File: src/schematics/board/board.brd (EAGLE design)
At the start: 50.8 x 35.6 mm, 23 parts, among them P1 PN61729-S, Q1 12MHz, U1 MCP17003302E/TO, U2 PIC18LF14K50-E-P

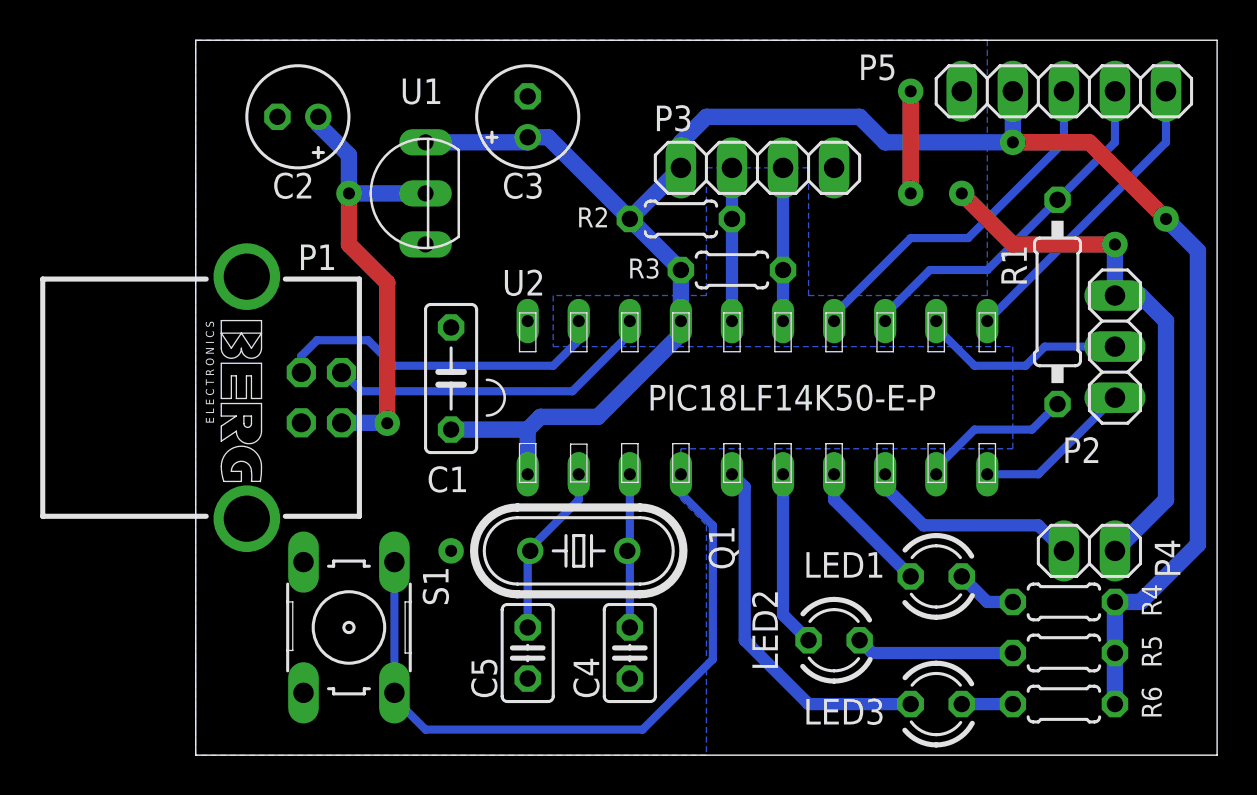
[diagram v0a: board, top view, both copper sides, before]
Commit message: Added UART pull-ups
Added pull-ups to the UART port, so that there are never mistaken signals.
They are not critical, but may help in keeping consistent values,
especially for the receiver.

Andrea Zoppi
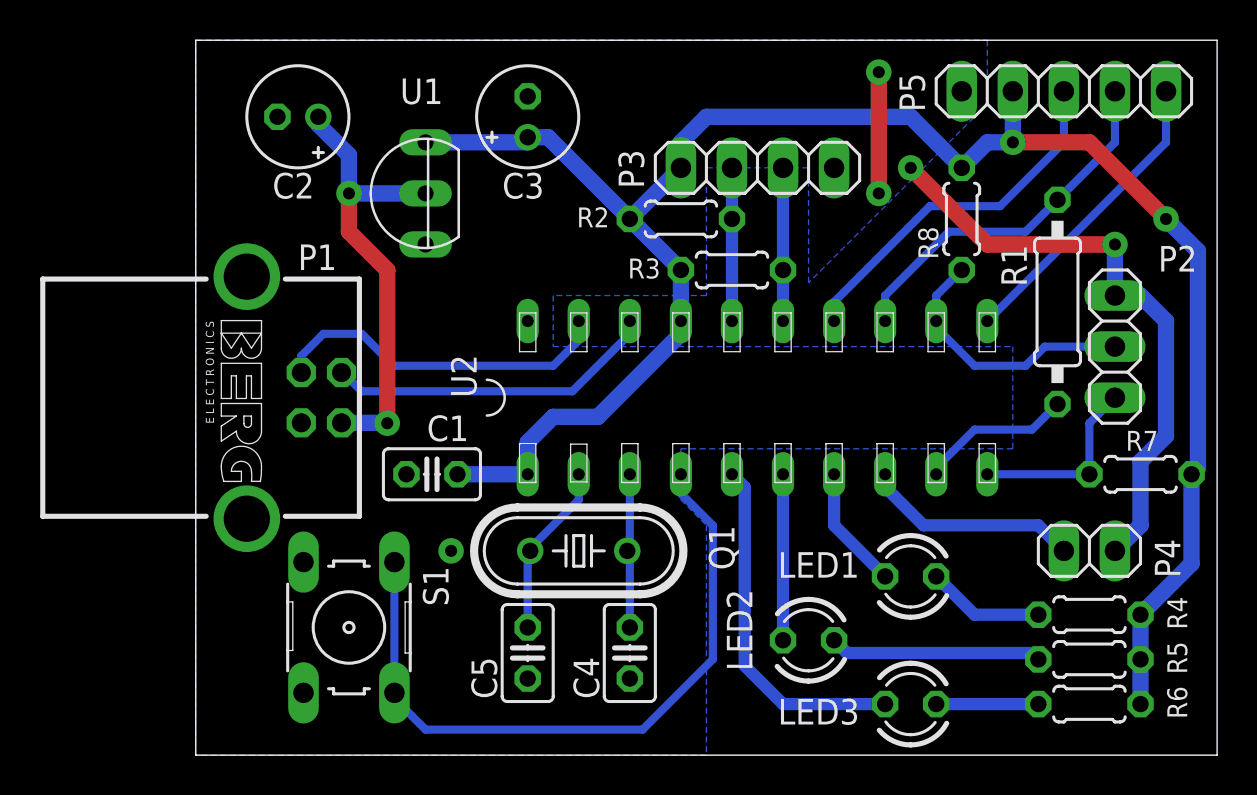
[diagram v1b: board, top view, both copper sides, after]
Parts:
- added R7, R8: 100k, rcl:0204/5
- C1: device rcl:C050-025X075 -> rcl:C025-025X050
- moved C1 4.86 mm to (11.7, 14.0), turned to 180 degrees
- moved R4 1.42 mm to (44.5, 6.99)
- moved R5 1.31 mm to (44.5, 4.76)
- moved R6 1.27 mm to (44.5, 2.54)
- moved LED2 1.27 mm to (30.5, 5.71)
- moved LED1 1.27 mm to (35.6, 8.89)
- moved LED3 1.27 mm to (35.6, 2.54)
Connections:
- net +3V3: now also R7.2, R8.2
- net RX: now also R8.1
- net TX: now also R7.1
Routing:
- net GND: track 31.8 -> 35.9 mm
- net RX: track 10.4 -> 13.5 mm
- net N$5: track 3.07 -> 5.87 mm
- net N$4: track 7.88 -> 10.6 mm
- net N$1: track 2.54 -> 5.08 mm
- net TX: track 7.93 -> 9.42 mm
- net +3V3: track 95.9 -> 95.0 mm
- net SDIO: track 17.8 -> 18.4 mm
- net RED: track 18.1 -> 17.6 mm
- net GREEN: track 6.66 -> 6.13 mm
- net YELLOW: track 8.78 -> 8.26 mm
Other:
- board text added: "1"
- board text added: "3V3"
- board text added: "5"
- board text added: "GND"
- board text added: "IN"
- board text added: "QA"
- board text added: "QB"
- board text added: "RX"
- board text added: "TX"

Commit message: Added user button pull-up
A pull-up resistor was added to the user button, because the built-in weak
pull-up of the MCU does not work properly at power-up.

Andrea Zoppi
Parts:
- added R9: 47k, rcl:0204/5
- R7, R8: value 100k -> 47k
- moved S1 1.80 mm to (6.35, 5.08)
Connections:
- net +3V3: now also R9.2
- net RST: now also R9.1
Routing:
- net +3V3: track 95.0 -> 102.7 mm
- net RST: track 34.6 -> 35.3 mm
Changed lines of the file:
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@@
 <layer number="27" name="tValues" color="7" fill="1" visible="yes" active="yes"/>
 <layer number="28" name="bValues" color="7" fill="1" visible="yes" active="yes"/>
-<layer number="29" name="tStop" color="7" fill="3" visible="yes" active="yes"/>
-<layer number="30" name="bStop" color="7" fill="6" visible="yes" active="yes"/>
-<layer number="31" name="tCream" color="7" fill="4" visible="yes" active="yes"/>
+<layer number="29" name="tStop" color="7" fill="3" visible="no" active="yes"/>
+<layer number="30" name="bStop" color="7" fill="6" visible="no" active="yes"/>
+<layer number="31" name="tCream" color="7" fill="4" visible="no" active="yes"/>
 <layer number="32" name="bCream" color="7" fill="5" visible="no" active="yes"/>
 <layer number="33" name="tFinish" color="6" fill="3" visible="no" active="yes"/>
@@
 <attribute name="NAME" x="25.527" y="11.43" size="1.27" layer="25" ratio="10" rot="R270"/>
 </element>
-<element name="S1" library="switch-omron" package="B3F-10XX" value="" x="7.62" y="6.35" rot="R270">
-<attribute name="OC_NEWARK" value="36M3542" x="-25.4" y="-12.7" size="1.778" layer="27" rot="R270" display="off"/>
-<attribute name="MPN" value="B3F-1000" x="-25.4" y="-12.7" size="1.778" layer="27" rot="R270" display="off"/>
-<attribute name="MF" value="" x="-25.4" y="-12.7" size="1.778" layer="27" rot="R270" display="off"/>
-<attribute name="OC_FARNELL" value="176432" x="-25.4" y="-12.7" size="1.778" layer="27" rot="R270" display="off"/>
+<element name="S1" library="switch-omron" package="B3F-10XX" value="" x="6.35" y="5.08" smashed="yes" rot="R270">
+<attribute name="OC_NEWARK" value="36M3542" x="-26.67" y="-13.97" size="1.778" layer="27" rot="R270" display="off"/>
+<attribute name="MPN" value="B3F-1000" x="-26.67" y="-13.97" size="1.778" layer="27" rot="R270" display="off"/>
+<attribute name="MF" value="" x="-26.67" y="-13.97" size="1.778" layer="27" rot="R270" display="off"/>
+<attribute name="OC_FARNELL" value="176432" x="-26.67" y="-13.97" size="1.778" layer="27" rot="R270" display="off"/>
+<attribute name="NAME" x="2.667" y="4.572" size="1.27" layer="25" ratio="10" rot="R90"/>
+<attribute name="VALUE" x="1.27" y="8.128" size="1.27" layer="27" ratio="10" rot="R270"/>
 </element>
 <element name="P2" library="pinhead" package="1X03" value="" x="45.72" y="20.32" smashed="yes" rot="R90">
@@
 </element>
 <element name="C4" library="rcl" package="C025-025X050" value="15p" x="21.59" y="5.08" smashed="yes" rot="R270">
-<attribute name="NAME" x="20.066" y="2.794" size="1.27" layer="25" ratio="10" rot="R90"/>
+<attribute name="NAME" x="20.8915" y="0.889" size="1.27" layer="25" ratio="10"/>
 </element>
 <element name="C5" library="rcl" package="C025-025X050" value="15p" x="16.51" y="5.08" smashed="yes" rot="R270">
-<attribute name="NAME" x="14.986" y="2.794" size="1.27" layer="25" ratio="10" rot="R90"/>
+<attribute name="NAME" x="15.494" y="0.889" size="1.27" layer="25" ratio="10"/>
 </element>
 <element name="R1" library="rcl" package="0207/10" value="100" x="42.8625" y="22.5425" smashed="yes" rot="R90">
@@
 <attribute name="VALUE" x="41.91" y="6.985" size="1.27" layer="27"/>
 </element>
-<element name="R7" library="rcl" package="0204/5" value="100k" x="46.99" y="13.97" smashed="yes">
+<element name="R7" library="rcl" package="0204/5" value="47k" x="46.99" y="13.97" smashed="yes">
 <attribute name="NAME" x="46.2534" y="15.1384" size="0.9906" layer="25" ratio="10"/>
 </element>
-<element name="R8" library="rcl" package="0204/5" value="100k" x="38.1" y="26.67" smashed="yes" rot="R90">
+<element name="R8" library="rcl" package="0204/5" value="47k" x="38.1" y="26.67" smashed="yes" rot="R90">
 <attribute name="NAME" x="36.9316" y="24.6634" size="0.9906" layer="25" ratio="10" rot="R90"/>
+</element>
+<element name="R9" library="rcl" package="0204/5" value="47k" x="12.7" y="3.81" smashed="yes" rot="R90">
+<attribute name="NAME" x="11.5316" y="3.0734" size="0.9906" layer="25" ratio="10" rot="R90"/>
 </element>
 </elements>
@@
 <wire x1="39.37" y1="25.4" x2="35.56" y2="29.21" width="0.8128" layer="1"/>
 <via x="35.56" y="29.21" extent="1-16" drill="0.6" diameter="1.27" shape="octagon"/>
-<via x="12.7" y="10.16" extent="1-16" drill="0.6" diameter="1.27" shape="octagon"/>
+<via x="19.05" y="6.985" extent="1-16" drill="0.6" diameter="1.27" shape="octagon"/>
 <polygon width="0.3048" layer="16">
 <vertex x="25.4" y="0"/>
@@
 <contactref element="R8" pad="2"/>
 <contactref element="R7" pad="2"/>
+<contactref element="R9" pad="2"/>
+<wire x1="13.0175" y1="13.97" x2="13.0175" y2="6.6675" width="0.8128" layer="16"/>
+<wire x1="13.0175" y1="6.6675" x2="12.7" y2="6.35" width="0.8128" layer="16"/>
 </signal>
 <signal name="N$2">
@@
 <wire x1="25.7175" y1="11.43" x2="24.13" y2="13.0175" width="0.4064" layer="16"/>
 <wire x1="24.13" y1="13.0175" x2="24.13" y2="13.97" width="0.4064" layer="16"/>
-<wire x1="9.8806" y1="9.6012" x2="9.8806" y2="3.0988" width="0.4064" layer="16"/>
-<wire x1="9.8806" y1="3.0988" x2="9.8806" y2="2.8194" width="0.6096" layer="16"/>
-<wire x1="9.8806" y1="2.8194" x2="11.43" y2="1.27" width="0.4064" layer="16"/>
-<wire x1="11.43" y1="1.27" x2="22.225" y2="1.27" width="0.4064" layer="16"/>
+<wire x1="8.6106" y1="8.3312" x2="8.6106" y2="1.8288" width="0.4064" layer="16"/>
+<wire x1="8.89" y1="1.27" x2="22.225" y2="1.27" width="0.4064" layer="16"/>
 <wire x1="22.225" y1="1.27" x2="25.7175" y2="4.7625" width="0.4064" layer="16"/>
+<contactref element="R9" pad="1"/>
+<wire x1="8.6106" y1="1.8288" x2="8.6106" y2="1.5494" width="0.4064" layer="16"/>
+<wire x1="8.6106" y1="1.5494" x2="8.89" y2="1.27" width="0.4064" layer="16"/>
+<wire x1="8.89" y1="1.27" x2="12.7" y2="1.27" width="0" layer="19" extent="16-16"/>
 </signal>
 <signal name="TX">

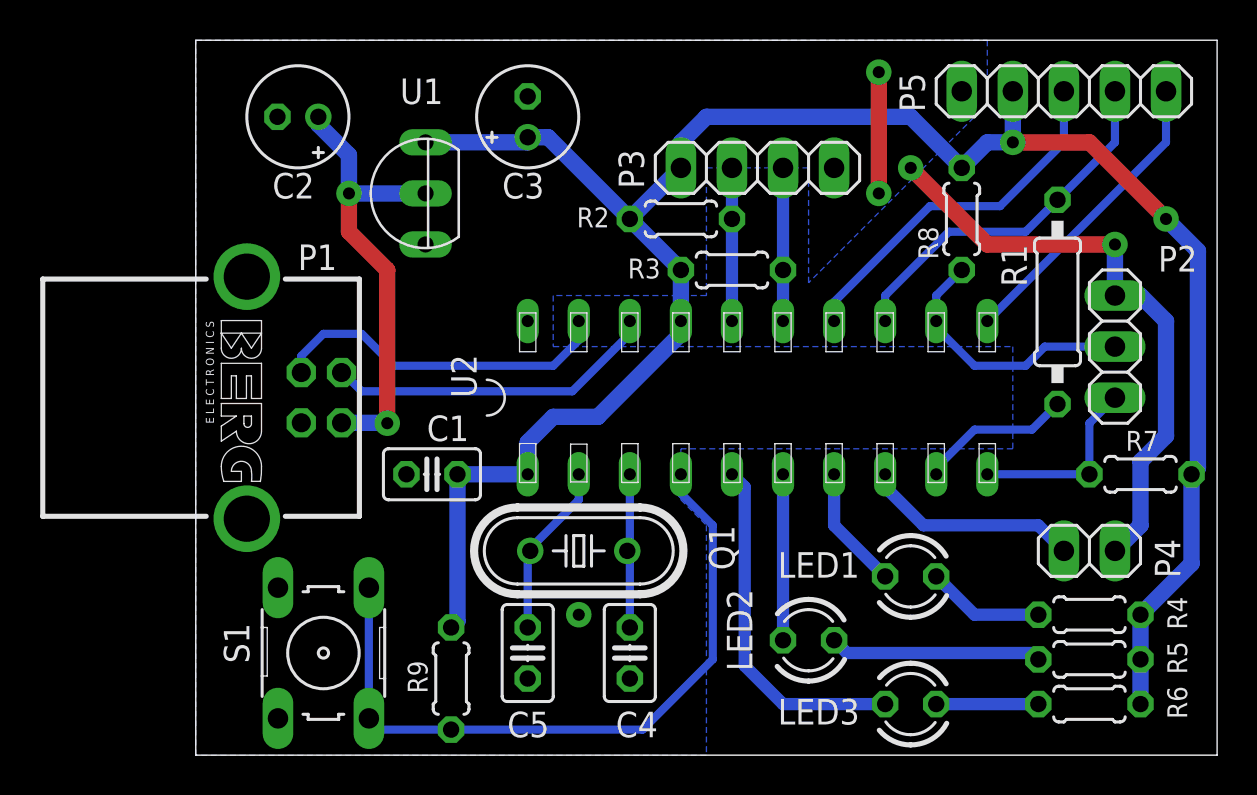
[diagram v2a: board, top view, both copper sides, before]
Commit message: Minor PCB fixes
Changed resistor values so that performance is improved, and the PIC
inputs can read correct pull-up values.

Andrea Zoppi
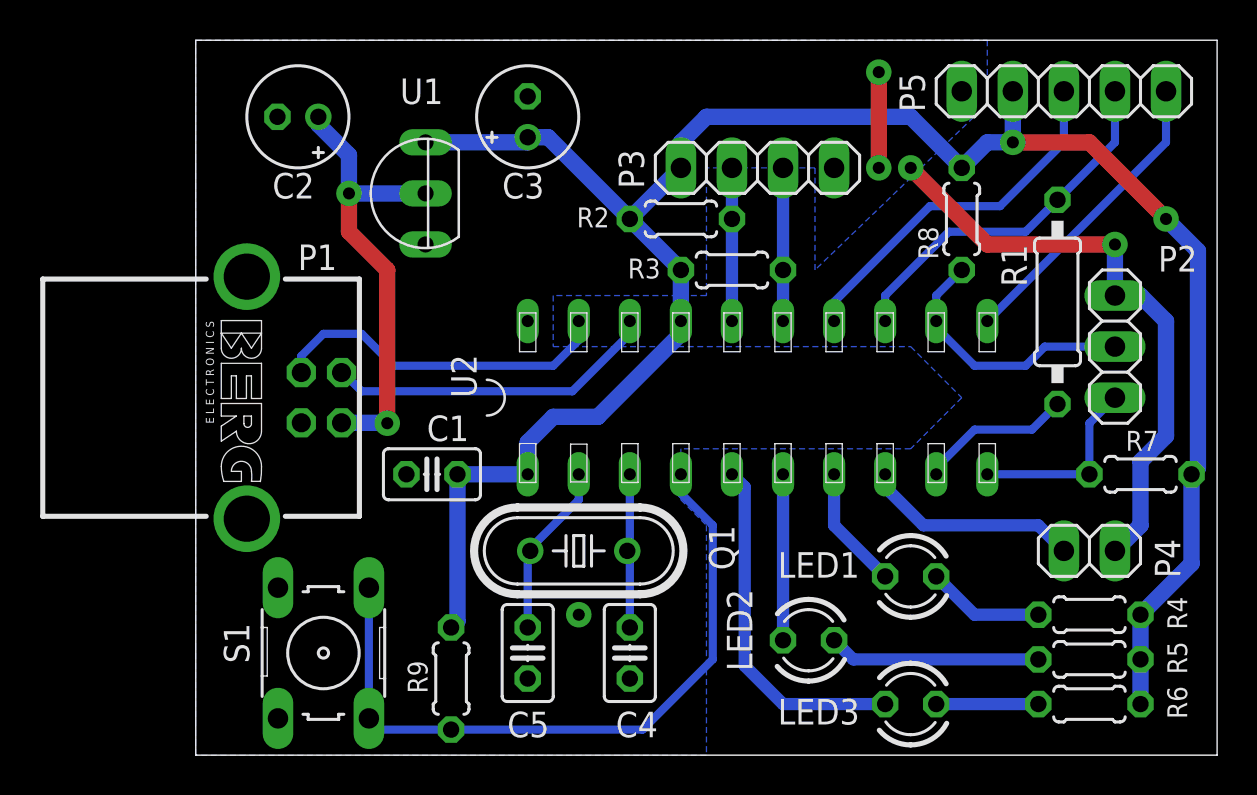
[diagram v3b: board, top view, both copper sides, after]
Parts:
- C2: value 22u -> 2u2
- R1: value 100 -> 150
- R7, R8, R9: value 47k -> 100k
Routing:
- net GND: track 35.9 -> 34.6 mm
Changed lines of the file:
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@@
 <attribute name="NAME" x="11.4935" y="15.621" size="1.27" layer="25" ratio="10"/>
 </element>
-<element name="C2" library="rcl" package="E2-5" value="22u" x="5.08" y="31.75" smashed="yes" rot="R180">
+<element name="C2" library="rcl" package="E2-5" value="2u2" x="5.08" y="31.75" smashed="yes" rot="R180">
 <attribute name="NAME" x="3.81" y="27.686" size="1.27" layer="25" ratio="10"/>
 </element>
@@
 <attribute name="NAME" x="15.494" y="0.889" size="1.27" layer="25" ratio="10"/>
 </element>
-<element name="R1" library="rcl" package="0207/10" value="100" x="42.8625" y="22.5425" smashed="yes" rot="R90">
+<element name="R1" library="rcl" package="0207/10" value="150" x="42.8625" y="22.5425" smashed="yes" rot="R90">
 <attribute name="NAME" x="41.3385" y="23.3045" size="1.27" layer="25" ratio="10" rot="R90"/>
 </element>
@@
 <attribute name="VALUE" x="41.91" y="6.985" size="1.27" layer="27"/>
 </element>
-<element name="R7" library="rcl" package="0204/5" value="47k" x="46.99" y="13.97" smashed="yes">
+<element name="R7" library="rcl" package="0204/5" value="100k" x="46.99" y="13.97" smashed="yes">
 <attribute name="NAME" x="46.2534" y="15.1384" size="0.9906" layer="25" ratio="10"/>
 </element>
-<element name="R8" library="rcl" package="0204/5" value="47k" x="38.1" y="26.67" smashed="yes" rot="R90">
+<element name="R8" library="rcl" package="0204/5" value="100k" x="38.1" y="26.67" smashed="yes" rot="R90">
 <attribute name="NAME" x="36.9316" y="24.6634" size="0.9906" layer="25" ratio="10" rot="R90"/>
 </element>
-<element name="R9" library="rcl" package="0204/5" value="47k" x="12.7" y="3.81" smashed="yes" rot="R90">
+<element name="R9" library="rcl" package="0204/5" value="100k" x="12.7" y="3.81" smashed="yes" rot="R90">
 <attribute name="NAME" x="11.5316" y="3.0734" size="0.9906" layer="25" ratio="10" rot="R90"/>
 </element>
@@
 <vertex x="39.37" y="35.56"/>
 <vertex x="39.37" y="32.385"/>
-<vertex x="30.48" y="23.495"/>
-<vertex x="30.48" y="29.21"/>
+<vertex x="30.7975" y="24.13"/>
+<vertex x="30.7975" y="29.21"/>
 <vertex x="25.4" y="29.21"/>
 <vertex x="25.4" y="22.86"/>
 <vertex x="17.78" y="22.86"/>
 <vertex x="17.78" y="20.32"/>
-<vertex x="40.64" y="20.32"/>
-<vertex x="40.64" y="15.24"/>
+<vertex x="35.56" y="20.32"/>
+<vertex x="38.1" y="17.78"/>
+<vertex x="35.56" y="15.24"/>
 <vertex x="24.13" y="15.24"/>
 <vertex x="24.13" y="12.7"/>
 <vertex x="25.4" y="11.43"/>
 </polygon>
-<wire x1="33.9725" y1="33.9725" x2="33.9725" y2="27.94" width="0.8128" layer="1"/>
+<wire x1="33.9725" y1="33.9725" x2="33.9725" y2="29.21" width="0.8128" layer="1"/>
 <via x="33.9725" y="33.9725" extent="1-16" drill="0.6" diameter="1.27" shape="octagon"/>
-<via x="33.9725" y="27.94" extent="1-16" drill="0.6" diameter="1.27" shape="octagon"/>
+<via x="33.9725" y="29.21" extent="1-16" drill="0.6" diameter="1.27" shape="octagon"/>
 </signal>
 <signal name="+5V">
@@
 <contactref element="R5" pad="1"/>
 <contactref element="LED2" pad="A"/>
-<wire x1="41.91" y1="4.7625" x2="41.5925" y2="5.08" width="0.6096" layer="16"/>
-<wire x1="41.5925" y1="5.08" x2="32.385" y2="5.08" width="0.6096" layer="16"/>
-<wire x1="32.385" y1="5.08" x2="31.75" y2="5.715" width="0.6096" layer="16"/>
+<wire x1="41.91" y1="4.7625" x2="32.7025" y2="4.7625" width="0.6096" layer="16"/>
+<wire x1="32.7025" y1="4.7625" x2="31.75" y2="5.715" width="0.6096" layer="16"/>
 </signal>
 <signal name="N$5">

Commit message: Incremental encoder and MOTION pins updated
Pins for incremental encoder signals (ENC_A and ENC_B), and the MOTION
signal have ben re-routed to the correct PIC pins, according to the
changes made in the latest commits.

Andrea Zoppi
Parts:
- moved R2 4.02 mm to (27.9, 25.4)
- moved R3 3.72 mm to (27.9, 27.6)
- moved P3 1.27 mm to (27.9, 30.5)
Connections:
- net ENC_A: now also U2.15; no longer U2.16
- net ENC_B: now also U2.14; no longer U2.15
- net MOTION: now also U2.16; no longer U2.14
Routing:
- net MOTION: track 18.2 -> 23.3 mm, vias 0 -> 2
- net ENC_A: track 7.62 -> 11.2 mm
- net ENC_B: track 7.62 -> 10.7 mm
- net +3V3: track 102.7 -> 104.4 mm
- net GND: track 34.6 -> 35.7 mm
